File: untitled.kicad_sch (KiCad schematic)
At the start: 8 parts, among them J3 USB_C_Receptacle_USB2.0_14P, J6 GPIO_INTERNAL_PINS, J7 GPIO_EXT_PINS, J8 Conn_01x03_Pin, SW4 5v_USB_EN

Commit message: board layout v1
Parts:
- removed J6: GPIO_INTERNAL_PINS, Connector_PinHeader_2.54mm:PinHeader_1x09_P2.54mm_Vertical, symbol PCM_4ms_Connector:Conn_01x09
- removed J7: GPIO_EXT_PINS, Connector_PinHeader_2.54mm:PinHeader_1x13_P2.54mm_Horizontal, symbol Connector_Generic:Conn_01x13
- added C3, C4: 0.1uF, Capacitor_SMD:C_1206_3216Metric, symbol Device:C
- added C5, C6: 22pF, Capacitor_SMD:C_1206_3216Metric, symbol Device:C
- added F2: Polyfuse_3A_15V, Fuse:Fuse_1812_4532Metric, symbol PCM_4ms_Regulator:Polyfuse_3A_15V
- added J15: Brake/FwRev, Connector_PinHeader_2.54mm:PinHeader_1x03_P2.54mm_Horizontal, symbol Connector:Conn_01x03_Pin
- added J16: 5v_in, TerminalBlock_MetzConnect:TerminalBlock_MetzConnect_Type011_RT05502HBWC_1x02_P5.00mm_Horizontal, symbol Connector:Screw_Terminal_01x02
- added J17: 3.3v_in, TerminalBlock_MetzConnect:TerminalBlock_MetzConnect_Type011_RT05502HBWC_1x02_P5.00mm_Horizontal, symbol Connector:Screw_Terminal_01x02
- added J18: 12v_in, TerminalBlock_MetzConnect:TerminalBlock_MetzConnect_Type011_RT05502HBWC_1x02_P5.00mm_Horizontal, symbol Connector:Screw_Terminal_01x02
- added J19: ~, SparkFun-Connectors:JST-2-PTH, symbol SparkFun-Connectors:CONN_02JST-PTH-2
- added J2: Raspberry_Pi_4, Connector_PinSocket_2.54mm:PinSocket_2x20_P2.54mm_Vertical, symbol Connector:Raspberry_Pi_4
- added J20: ~, SparkFun-Connectors:JST-6-SMD-1.25MM-LOCKING, symbol SparkFun-Connectors:CONN_06JST-SMD-LOCKING
- added J21: CAN, Connector_JST:JST_EH_B2B-EH-A_1x02_P2.50mm_Vertical, symbol Connector:Screw_Terminal_01x02
- added J23: 5v_rail, Connector_PinHeader_2.54mm:PinHeader_1x05_P2.54mm_Vertical, symbol Connector:Conn_01x05_Pin
- added J24: 3.3v_rail, Connector_PinHeader_2.54mm:PinHeader_1x05_P2.54mm_Vertical, symbol Connector:Conn_01x05_Pin
- added J25: 12v_rail, Connector_PinHeader_2.54mm:PinHeader_1x05_P2.54mm_Vertical, symbol Connector:Conn_01x05_Pin
- added J26: GND_rail, Connector_PinHeader_2.54mm:PinHeader_1x05_P2.54mm_Vertical, symbol Connector:Conn_01x05_Pin
- added J27: 12v_rail_f, Connector_PinSocket_2.54mm:PinSocket_1x05_P2.54mm_Vertical, symbol Connector:Conn_01x05_Socket
- added J28: 3.3v_rail_f, Connector_PinSocket_2.54mm:PinSocket_1x05_P2.54mm_Vertical, symbol Connector:Conn_01x05_Socket
- added J29: 5v_rail_f, Connector_PinSocket_2.54mm:PinSocket_1x05_P2.54mm_Vertical, symbol Connector:Conn_01x05_Socket
- added J30: GND_rail_f, Connector_PinSocket_2.54mm:PinSocket_1x05_P2.54mm_Vertical, symbol Connector:Conn_01x05_Socket
- added J6: Conn_01x07, Connector_PinHeader_2.54mm:PinHeader_1x07_P2.54mm_Vertical, symbol Connector_Generic:Conn_01x07
- added J7: Conn_01x05, Connector_PinHeader_2.54mm:PinHeader_1x05_P2.54mm_Vertical, symbol Connector_Generic:Conn_01x05
- added JP1: CAN_TXD_SEL, Jumper:SolderJumper-3_P1.3mm_Bridged12_Pad1.0x1.5mm, symbol Jumper:SolderJumper_3_Bridged12
- added JP2: CAN_RXD_SEL, Jumper:SolderJumper-3_P1.3mm_Bridged12_Pad1.0x1.5mm, symbol Jumper:SolderJumper_3_Bridged12
- added R1: 10k, Resistor_SMD:R_1206_3216Metric, symbol Device:R_US
- added U6: MCP2515-xSO, Package_SO:SOIC-18W_7.5x11.6mm_P1.27mm, symbol Interface_CAN_LIN:MCP2515-xSO
- added U7: SN65HVD230, Package_SO:SOIC-8_3.9x4.9mm_P1.27mm, symbol Interface_CAN_LIN:SN65HVD230
- added Y1: 16MHz, Crystal:Crystal_HC18-U_Vertical, symbol Device:Crystal
- J8: value Conn_01x03_Pin -> Throttle Connector
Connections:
- net ERR_HIGH_L is gone; now on net GPIO_INTERNAL_8: J4.67 (G8)
- net ERR_LOW_L is gone; now on net GPIO_INTERNAL_7: J4.69 (G7/BUS7)
- net +5V: now also J4.9 (USB_VIN), F2.2, J16.1 (Pin_1), J23.1 (Pin_1), J23.2 (Pin_2), J23.3 (Pin_3), J23.4 (Pin_4), J23.5 (Pin_5), J29.1 (Pin_1), J29.2 (Pin_2), J29.3 (Pin_3), J29.4 (Pin_4), J29.5 (Pin_5)
- net GND: now also C3.2, C4.2, J16.2 (Pin_2), J17.2 (Pin_2), J18.2 (Pin_2), J2.14 (GND), J2.20 (GND), J2.25 (GND), J2.30 (GND), J2.34 (GND), J2.39 (GND), J2.6 (GND), J2.9 (GND), J26.1 (Pin_1), J26.2 (Pin_2), J26.3 (Pin_3), J26.4 (Pin_4), J26.5 (Pin_5), J30.1 (Pin_1), J30.2 (Pin_2), J30.3 (Pin_3), J30.4 (Pin_4), J30.5 (Pin_5), R1.1, U6.9 (VSS), U7.2 (GND)
- net GPIO_EXT_0: now also J20.1, J7.5 (Pin_5)
- net GPIO_EXT_1: now also J20.6, J7.4 (Pin_4)
- net GPIO_EXT_2: now also J20.5, J7.3 (Pin_3)
- net GPIO_EXT_3: now also J20.4, J7.2 (Pin_2)
- net GPIO_EXT_4: now also J20.3, J7.1 (Pin_1)
- net GPIO_EXT_5: now also J20.2
- net GPIO_INTERNAL_3: now also J6.4 (Pin_4)
- net GPIO_INTERNAL_4: now also J6.3 (Pin_3)
- net GPIO_INTERNAL_5: now also J6.2 (Pin_2)
- net GPIO_INTERNAL_6: now also J6.1 (Pin_1)
- net ~{BOOT_uMOD}: now reaches J4.11 (~{BOOT})
- net uMod_TX1: now reaches J4.17 (TX1)
- net uMod_TX1: now also J2.10 (GPIO15/UART_RXD)
- net uMod_RX1: now reaches J4.19 (RX1)
- net uMod_RX1: now also J2.8 (GPIO14/UART_TXD)
- net +3.3V: now reaches J4.2 (3.3V), J4.74 (3.3V)
- net +3.3V: now also C3.1, C4.1, J17.1 (Pin_1), J24.1 (Pin_1), J24.2 (Pin_2), J24.3 (Pin_3), J24.4 (Pin_4), J24.5 (Pin_5), J28.1 (Pin_1), J28.2 (Pin_2), J28.3 (Pin_3), J28.4 (Pin_4), J28.5 (Pin_5), U6.18 (VDD), U7.3 (VCC)
- net TX_DRV_L: now reaches J4.20 (RX2)
- net RX_DRV_L: now reaches J4.22 (TX2)
- net CAN_RXD: now reaches J4.41 (CAN-RX)
- net CAN_RXD: now also JP2.1 (A)
- net CAN_TXD: now reaches J4.43 (CAN-TX)
- net CAN_TXD: now also JP1.3 (B)
- net GPIO_INTERNAL_0 renamed ~{E-STOP}
- net ~{E-STOP}: now also J19.2, J6.7 (Pin_7)
- net GPIO_INTERNAL_1 renamed ERR_L
- net ERR_L: now also J6.6 (Pin_6)
- net GPIO_INTERNAL_2 renamed ~{E-STOP-TRIG}
- net ~{E-STOP-TRIG}: now also J19.1, J6.5 (Pin_5)
- net RST renamed ~{RESET_uMOD}
- net SCL_MCTRL_L: no longer names the net of J4.53 (I2C_SCL1)
- net SDA _MCTRL_L: no longer names the net of J4.51 (I2C_SDA1)
- new net: R1.2, U6.17 (~{RESET})
- new net: C5.1, U6.7 (OSC2)
- new net: C6.1, U6.8 (OSC1)
- new net: J2.1 (3V3), J2.17 (3V3)
- new net: F2.1, J2.2 (5V), J2.4 (5V)
- new net: C5.2, Y1.2
- new net: J21.1 (Pin_1), U7.7 (CANH)
- new net: J21.2 (Pin_2), U7.6 (CANL)
- new net: JP1.1 (A), U7.1 (D)
- new net: JP2.3 (B), U7.4 (R)
- new net: C6.2, Y1.1
- new net +12V: J18.1 (Pin_1), J25.1 (Pin_1), J25.2 (Pin_2), J25.3 (Pin_3), J25.4 (Pin_4), J25.5 (Pin_5), J27.1 (Pin_1), J27.2 (Pin_2), J27.3 (Pin_3), J27.4 (Pin_4), J27.5 (Pin_5)
- new net Brk_hi: J15.1 (Pin_1)
- new net Brk_low: J15.2 (Pin_2)
- new net CAN_CS: J2.24 (~{CE0}_SPI0/GPIO08), U6.16 (~{CS})
- new net CAN_MISO: J2.21 (MISO_SPI0/GPIO09), U6.15 (SO)
- new net CAN_MOSI: J2.19 (MOSI_SPI0/GPIO10), U6.14 (SI)
- new net CAN_RXD_PI: JP2.2 (C), U6.2 (RXCAN)
- new net CAN_SCK: J2.23 (SCLK_SPI0/GPIO11), U6.13 (SCK)
- new net CAN_SPD: U7.8 (Rs)
- new net CAN_TXD_PI: JP1.2 (C), U6.1 (TXCAN)
- new net Fw/Rv: J15.3 (Pin_3)
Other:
- note added: "DOUBLE CHECK POSITION AND VOLTAGE ON INTERFACE BOARD, ALSO OTHER CONNECTOR"
- note added: "E-Stop"
- note added: "INTERFACE PCB"
- title: (none) -> AAV edge connectors
- moved on the sheet: J8

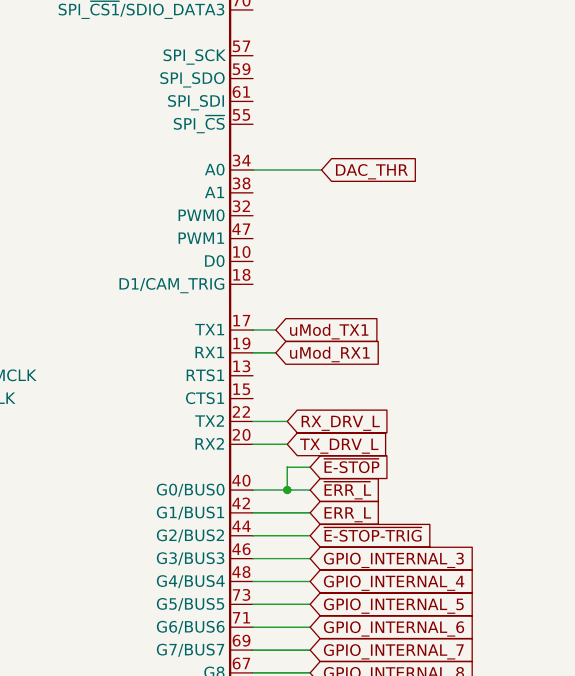
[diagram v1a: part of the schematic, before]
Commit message: add solder jumpers
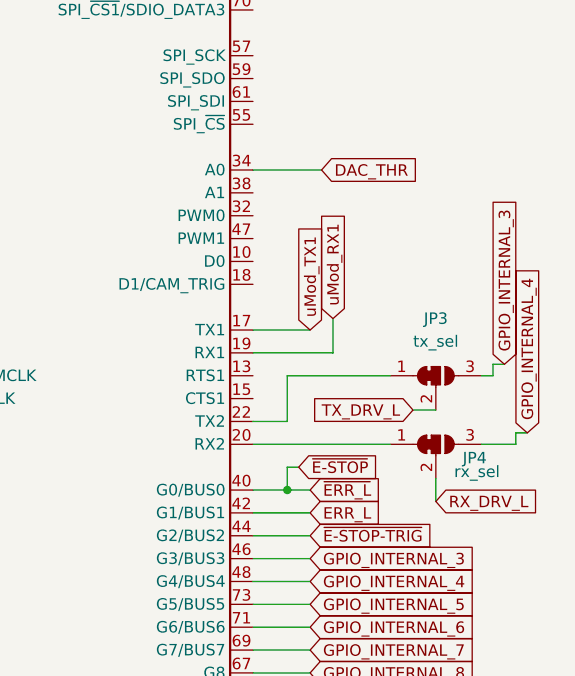
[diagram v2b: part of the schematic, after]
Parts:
- added JP3: tx_sel, symbol Jumper:SolderJumper_3_Bridged12
- added JP4: rx_sel, symbol Jumper:SolderJumper_3_Bridged12
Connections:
- net GPIO_INTERNAL_3: now also JP3.3 (B)
- net GPIO_INTERNAL_4: now also JP4.3 (B)
- net RX_DRV_L: now also JP4.2 (C); no longer J4.22 (TX2)
- net TX_DRV_L: now also JP3.2 (C); no longer J4.20 (RX2)
- new net: J4.20 (RX2), JP4.1 (A)
- new net: J4.22 (TX2), JP3.1 (A)

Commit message: i2c address fix and logo
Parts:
- JP3, JP4: footprint (none) -> Jumper:SolderJumper-3_P1.3mm_Bridged12_Pad1.0x1.5mm
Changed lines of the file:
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@@
 			)
 		)
-		(property "Footprint" ""
+		(property "Footprint" "Jumper:SolderJumper-3_P1.3mm_Bridged12_Pad1.0x1.5mm"
 			(at 273.05 114.3 0)
 			(effects
@@
 			)
 		)
-		(property "Footprint" ""
+		(property "Footprint" "Jumper:SolderJumper-3_P1.3mm_Bridged12_Pad1.0x1.5mm"
 			(at 273.05 106.68 0)
 			(effects

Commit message: Review and fixes from reliability and safety team
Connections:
- net +3.3V: now also R1.1
- net GND: now also C5.2, C6.1; no longer R1.1
- net RESET: now reaches R1.2, U6.17 (~{RESET})
- net XTAL_2: now reaches C5.1, U6.7 (OSC2)
- net XTAL_2: now also Y1.1
- net XTAL_1: now reaches U6.8 (OSC1)
- net XTAL_1: now also C6.2, Y1.2; no longer C6.1
- no-connect marks 0 -> 55
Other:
- moved on the sheet: C5, C6, R1, Y1

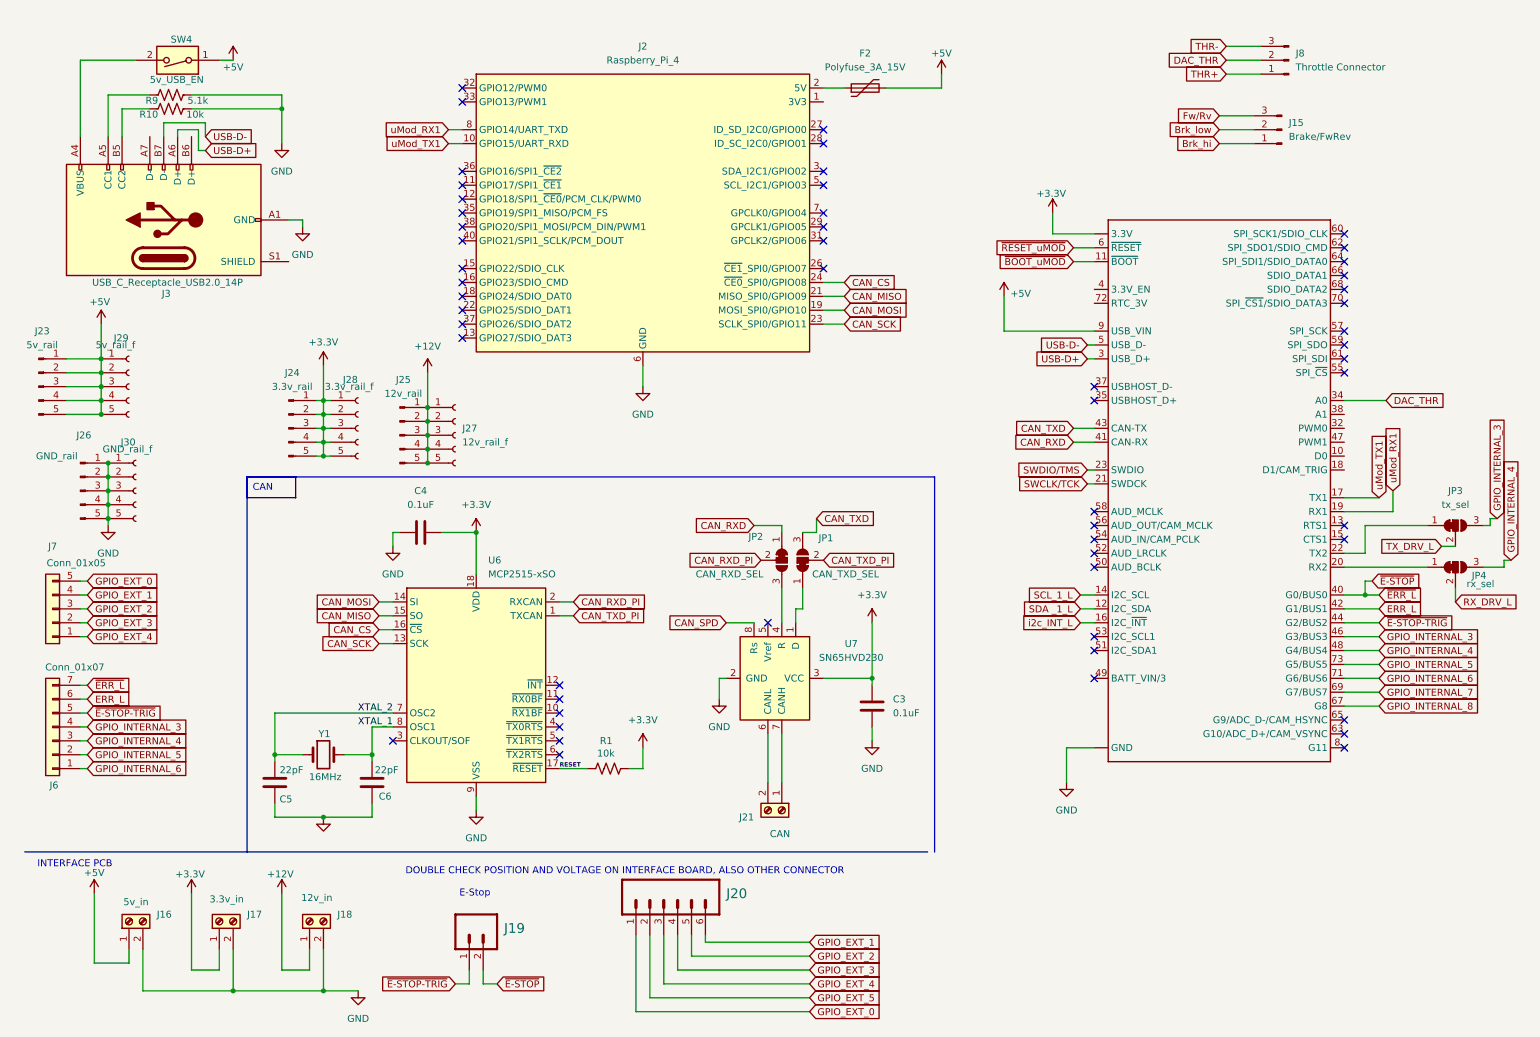
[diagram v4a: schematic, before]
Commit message: added micromod breakout and fixed voltage divider
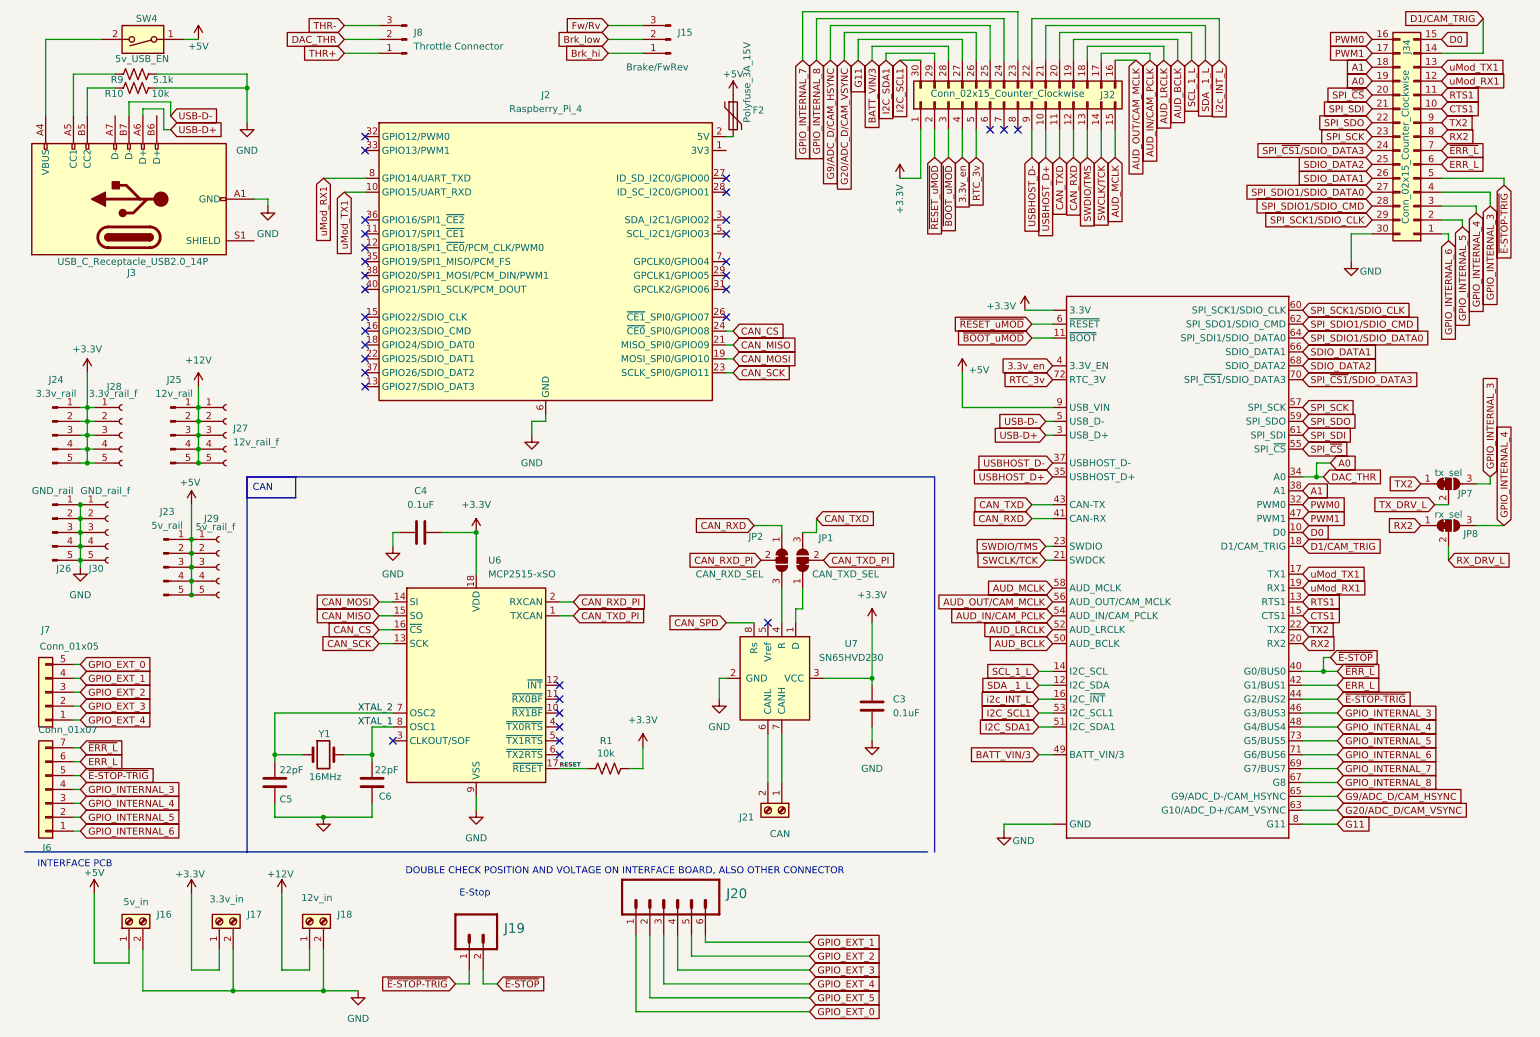
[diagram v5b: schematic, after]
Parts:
- removed J4: ~, SparkFun-MicroMod:M.2-CONNECTOR-E, symbol SparkFun-MicroMod:MICROMOD-2222-C
- removed JP3: tx_sel, Jumper:SolderJumper-3_P1.3mm_Bridged12_Pad1.0x1.5mm, symbol Jumper:SolderJumper_3_Bridged12
- removed JP4: rx_sel, Jumper:SolderJumper-3_P1.3mm_Bridged12_Pad1.0x1.5mm, symbol Jumper:SolderJumper_3_Bridged12
- added J32, J34: Conn_02x15_Counter_Clockwise, Connector_PinHeader_2.54mm:PinHeader_2x15_P2.54mm_Vertical, symbol Connector_Generic:Conn_02x15_Counter_Clockwise
- added J33: ~, SparkFun-MicroMod:M.2-CONNECTOR-E, symbol SparkFun-MicroMod:MICROMOD-2222-C
- added JP7: tx_sel, Jumper:SolderJumper-3_P1.3mm_Bridged12_Pad1.0x1.5mm, symbol Jumper:SolderJumper_3_Bridged12
- added JP8: rx_sel, Jumper:SolderJumper-3_P1.3mm_Bridged12_Pad1.0x1.5mm, symbol Jumper:SolderJumper_3_Bridged12
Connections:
- net +3.3V: now also J32.1 (Pin_1), J33.2 (3.3V), J33.74 (3.3V)
- net +5V: now also F2.1, J33.9 (USB_VIN); no longer F2.2
- net CAN_RXD: now also J32.12 (Pin_12), J33.41 (CAN-RX)
- net CAN_TXD: now also J32.11 (Pin_11), J33.43 (CAN-TX)
- net ERR_L: now also J33.42 (G1/BUS1), J34.6 (Pin_6)
- net GND: now also J33.1 (GND), J33.33 (GND), J33.36 (GND), J33.39 (GND), J33.45 (GND), J33.7 (GND), J33.75 (GND), J34.30 (Pin_30)
- net GPIO_INTERNAL_3: now also J33.46 (G3/BUS3), J34.4 (Pin_4), JP7.3 (B)
- net GPIO_INTERNAL_4: now also J33.48 (G4/BUS4), J34.3 (Pin_3), JP8.3 (B)
- net GPIO_INTERNAL_5: now also J33.73 (G5/BUS5), J34.2 (Pin_2)
- net GPIO_INTERNAL_6: now also J33.71 (G6/BUS6), J34.1 (Pin_1)
- net GPIO_INTERNAL_7: now also J32.23 (Pin_23), J33.69 (G7/BUS7)
- net GPIO_INTERNAL_8: now also J32.24 (Pin_24), J33.67 (G8)
- net RX_DRV_L: now also JP8.2 (C)
- net SCL_1_L: now also J32.20 (Pin_20), J33.14 (I2C_SCL)
- net SDA _1_L: now also J32.21 (Pin_21), J33.12 (I2C_SDA)
- net SWCLK/TCK: now also J32.14 (Pin_14), J33.21 (SWDCK)
- net SWDIO/TMS: now also J32.13 (Pin_13), J33.23 (SWDIO)
- net TX_DRV_L: now also JP7.2 (C)
- net USB-D+: now also J33.3 (USB_D+)
- net USB-D-: now also J33.5 (USB_D-)
- net i2c_INT_L: now also J32.22 (Pin_22), J33.16 (I2C_~{INT})
- net uMod_RX1: now also J33.19 (RX1), J34.12 (Pin_12)
- net uMod_TX1: now also J33.17 (TX1), J34.13 (Pin_13)
- net ~{BOOT_uMOD}: now also J32.3 (Pin_3), J33.11 (~{BOOT})
- net ~{E-STOP-TRIG}: now also J33.44 (G2/BUS2), J34.5 (Pin_5)
- net ~{E-STOP}: now also J33.40 (G0/BUS0), J34.7 (Pin_7)
- net ~{RESET_uMOD}: now also J32.2 (Pin_2), J33.6 (~{RESET})
- net at J2.2 (5V), J2.4 (5V): now also F2.2; no longer F2.1
- net DAC_THR renamed A0
- net A0: now also J33.34 (A0), J34.19 (Pin_19)
- new net 3.3v_en: J32.4 (Pin_4), J33.4 (3.3V_EN)
- new net A1: J33.38 (A1), J34.18 (Pin_18)
- new net AUD_BCLK: J32.19 (Pin_19), J33.50 (AUD_BCLK)
- new net AUD_IN/CAM_PCLK: J32.17 (Pin_17), J33.54 (AUD_IN/CAM_PCLK)
- new net AUD_LRCLK: J32.18 (Pin_18), J33.52 (AUD_LRCLK)
- new net AUD_MCLK: J32.15 (Pin_15), J33.58 (AUD_MCLK)
- new net AUD_OUT/CAM_MCLK: J32.16 (Pin_16), J33.56 (AUD_OUT/CAM_MCLK)
- new net BATT_VIN/3: J32.28 (Pin_28), J33.49 (BATT_VIN/3)
- new net CTS1: J33.15 (CTS1), J34.10 (Pin_10)
- new net D0: J33.10 (D0), J34.15 (Pin_15)
- new net D1/CAM_TRIG: J33.18 (D1/CAM_TRIG), J34.14 (Pin_14)
- new net G11: J32.27 (Pin_27), J33.8 (G11)
- new net G20/ADC_D/CAM_VSYNC: J32.26 (Pin_26), J33.63 (G10/ADC_D+/CAM_VSYNC)
- new net G9/ADC_D/CAM_HSYNC: J32.25 (Pin_25), J33.65 (G9/ADC_D-/CAM_HSYNC)
- new net I2C_SCL1: J32.30 (Pin_30), J33.53 (I2C_SCL1)
- new net I2C_SDA1: J32.29 (Pin_29), J33.51 (I2C_SDA1)
- new net PWM0: J33.32 (PWM0), J34.16 (Pin_16)
- new net PWM1: J33.47 (PWM1), J34.17 (Pin_17)
- new net RTC_3v: J32.5 (Pin_5), J33.72 (RTC_3V)
- new net RTS1: J33.13 (RTS1), J34.11 (Pin_11)
- new net RX2: J33.20 (RX2), J34.8 (Pin_8), JP8.1 (A)
- new net SDIO_DATA1: J33.66 (SDIO_DATA1), J34.26 (Pin_26)
- new net SDIO_DATA2: J33.68 (SDIO_DATA2), J34.25 (Pin_25)
- new net SPI_SCK: J33.57 (SPI_SCK), J34.23 (Pin_23)
- new net SPI_SCK1/SDIO_CLK: J33.60 (SPI_SCK1/SDIO_CLK), J34.29 (Pin_29)
- new net SPI_SDI: J33.61 (SPI_SDI), J34.21 (Pin_21)
- new net SPI_SDIO1/SDIO_CMD: J33.62 (SPI_SDO1/SDIO_CMD), J34.28 (Pin_28)
- new net SPI_SDIO1/SDIO_DATA0: J33.64 (SPI_SDI1/SDIO_DATA0), J34.27 (Pin_27)
- new net SPI_SDO: J33.59 (SPI_SDO), J34.22 (Pin_22)
- new net SPI_~{CS1}/SDIO_DATA3: J33.70 (SPI_~{CS1}/SDIO_DATA3), J34.24 (Pin_24)
- new net SPI_~{CS}: J33.55 (SPI_~{CS}), J34.20 (Pin_20)
- new net TX2: J33.22 (TX2), J34.9 (Pin_9), JP7.1 (A)
- new net USBHOST_D+: J32.10 (Pin_10), J33.35 (USBHOST_D+)
- new net USBHOST_D-: J32.9 (Pin_9), J33.37 (USBHOST_D-)
- no-connect marks 55 -> 33
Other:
- company: (none) -> Charlie Wadds
- moved on the sheet: F2, J15, J2, J23, J24, J25, J26, J27, J28, J29, J3, J30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

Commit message: pre-fab review & cleanup
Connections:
- net CANH: now reaches J21.1 (Pin_1), U7.7 (CANH)
- net CANL: now reaches J21.2 (Pin_2), U7.6 (CANL)
- no-connect marks 33 -> 34
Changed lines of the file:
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@@
+	)
+	(no_connect
+		(at 139.7 38.1)
 	)
 	(no_connect
@@
 		(effects
 			(font
+				(size 1.27 1.27)
+			)
+			(justify right bottom)
+		)
+	)
+	(label "CANL"
+		(at 147.32 144.78 270)
+		(effects
+			(font
+				(size 1.27 1.27)
+			)
+			(justify right bottom)
+		)
+	)
+	(label "CANH"
+		(at 149.86 144.78 270)
+		(effects
+			(font

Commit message: changed LED
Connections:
- net CANH: no longer names the net of J21.1 (Pin_1), U7.7 (CANH)
- net CANL: no longer names the net of J21.2 (Pin_2), U7.6 (CANL)
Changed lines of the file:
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@@
+	)
+	(no_connect
+		(at 139.7 58.42)
+	)
+	(no_connect
+		(at 139.7 53.34)
+	)
+	(no_connect
+		(at 109.22 148.59)
+	)
+	(no_connect
+		(at 139.7 63.5)
 	)
 	(no_connect
 		(at 139.7 38.1)
-	)
-	(no_connect
-		(at 139.7 58.42)
-	)
-	(no_connect
-		(at 139.7 53.34)
-	)
-	(no_connect
-		(at 109.22 148.59)
-	)
-	(no_connect
-		(at 139.7 63.5)
 	)
 	(no_connect
@@
 		(effects
 			(font
-				(size 1.27 1.27)
-			)
-			(justify right bottom)
-		)
-	)
-	(label "CANL"
-		(at 147.32 144.78 270)
-		(effects
-			(font
-				(size 1.27 1.27)
-			)
-			(justify right bottom)
-		)
-	)
-	(label "CANH"
-		(at 149.86 144.78 270)
-		(effects
-			(font

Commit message: new branch with fixes
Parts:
- removed J3: USB_C_Receptacle_USB2.0_14P, Connector_USB:USB_C_Receptacle_Amphenol_124019772112A, symbol Connector:USB_C_Receptacle_USB2.0_14P
- added J31: USB4520-03-0-A_REVA, USB4105_GF_A:GCT_USB4105-GF-A, symbol USB4520-03-0-A_REVA:USB4520-03-0-A_REVA
- added R16, R2: 10k, Resistor_SMD:R_1206_3216Metric, symbol Device:R_US
- R10: value 10k -> 5.1k
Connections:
- net A0: now also R2.2; no longer J8.2 (Pin_2)
- net CAN_RXD_PI: now also JP2.3 (B); no longer JP2.2 (C)
- net CAN_TXD: now also JP1.1 (A); no longer JP1.3 (B)
- net CAN_TXD_PI: now also JP1.3 (B); no longer JP1.2 (C)
- net GND: now also J31.A1_B12 (GND_A), J31.B1_A12 (GND_B)
- net USB-D+: now also J31.A6 (DP1), J31.B6 (DP2)
- net USB-D-: now also J31.A7 (DN1), J31.B7 (DN2)
- net at SW4.2: now also J31.A4_B9 (VBUS_A), J31.B4_A9 (VBUS_B)
- net at R9.1: now also J31.A5 (CC1)
- net at R10.1: now also J31.B5 (CC2)
- net at U7.1 (D): now also JP1.2 (C); no longer JP1.1 (A)
- net at U7.4 (R): now also JP2.2 (C); no longer JP2.3 (B)
- new net: R16.2, R2.1
- new net DAC_THR: J8.2 (Pin_2), R16.1
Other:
- moved on the sheet: J23, J24, J25, J26, J27, J28, J29, J30, JP1, R10
